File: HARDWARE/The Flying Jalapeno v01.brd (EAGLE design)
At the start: 73.7 x 72.4 mm, 96 parts, among them Q2 MMBT2222A, Q3 NDP6020P, Q4 MMBT2222A, Q5 NDP6020P, Q6 BSS138, 200mA/50V, Q7 BSS138, 200mA/50V, U1 ATMEGA2560AU, U2 LM1117, U3 LM1117, U4 LM1117, Y1 16MHZ

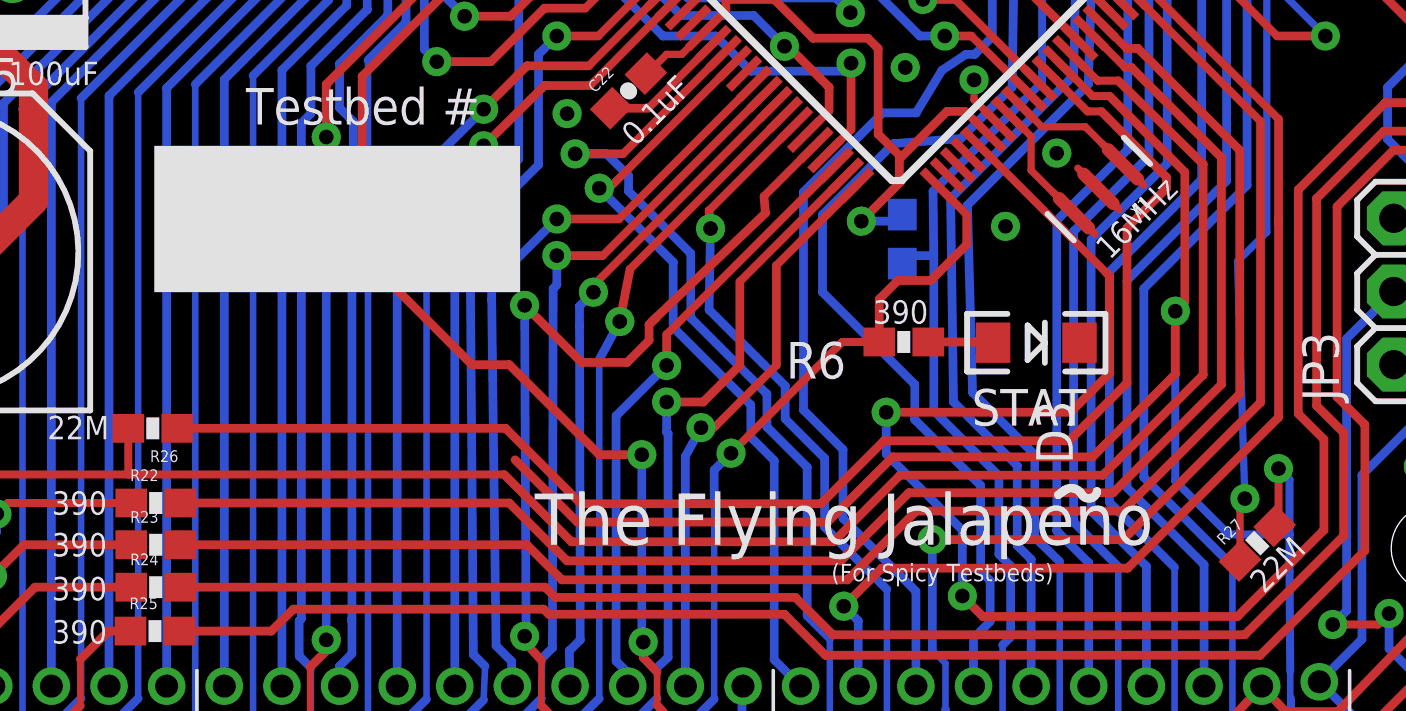
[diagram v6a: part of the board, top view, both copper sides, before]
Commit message: Fixed Rogue trace off of capsense2
Thanks for catching this in your review Kade!
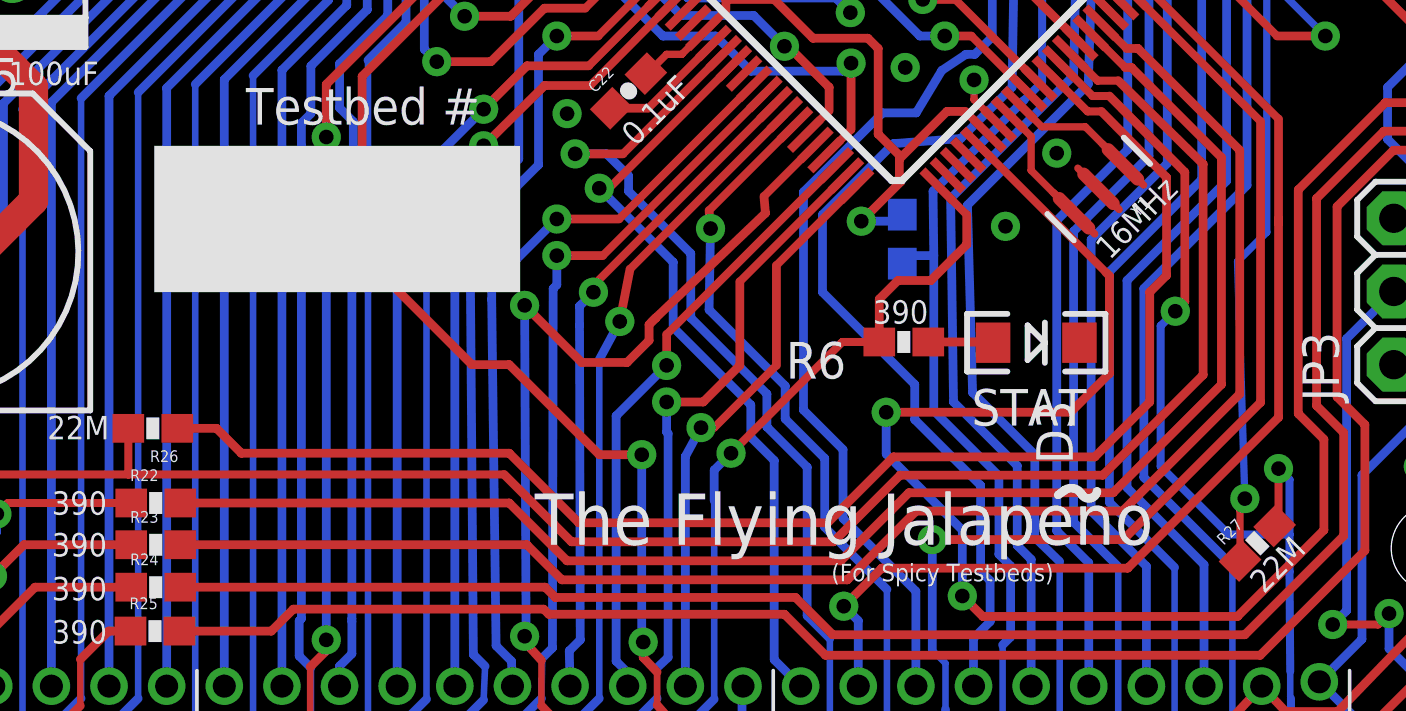
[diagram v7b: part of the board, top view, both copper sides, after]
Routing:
- net 46/CAPSENSE2: track 66.3 -> 38.6 mm
- net 47/CAPRETURN1: track 49.0 -> 50.4 mm
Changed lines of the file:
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@@
 <setting verticaltext="up"/>
 </settings>
-<grid distance="0.05" unitdist="inch" unit="inch" style="lines" multiple="1" display="yes" altdistance="0.001" altunitdist="inch" altunit="inch"/>
+<grid distance="0.05" unitdist="inch" unit="inch" style="lines" multiple="1" display="yes" altdistance="0.005" altunitdist="inch" altunit="inch"/>
 <layers>
-<layer number="1" name="Top" color="4" fill="1" visible="no" active="yes"/>
+<layer number="1" name="Top" color="4" fill="1" visible="yes" active="yes"/>
 <layer number="2" name="Route2" color="1" fill="3" visible="no" active="no"/>
 <layer number="3" name="Route3" color="4" fill="3" visible="no" active="no"/>
@@
 <layer number="14" name="Route14" color="1" fill="6" visible="no" active="no"/>
 <layer number="15" name="Route15" color="4" fill="6" visible="no" active="no"/>
-<layer number="16" name="Bottom" color="1" fill="1" visible="no" active="yes"/>
+<layer number="16" name="Bottom" color="1" fill="1" visible="yes" active="yes"/>
 <layer number="17" name="Pads" color="2" fill="1" visible="yes" active="yes"/>
 <layer number="18" name="Vias" color="2" fill="1" visible="yes" active="yes"/>
-<layer number="19" name="Unrouted" color="6" fill="1" visible="no" active="yes"/>
+<layer number="19" name="Unrouted" color="6" fill="1" visible="yes" active="yes"/>
 <layer number="20" name="Dimension" color="15" fill="1" visible="yes" active="yes"/>
 <layer number="21" name="tPlace" color="16" fill="1" visible="yes" active="yes"/>
-<layer number="22" name="bPlace" color="14" fill="1" visible="no" active="yes"/>
-<layer number="23" name="tOrigins" color="15" fill="1" visible="no" active="yes"/>
-<layer number="24" name="bOrigins" color="15" fill="1" visible="no" active="yes"/>
+<layer number="22" name="bPlace" color="14" fill="1" visible="yes" active="yes"/>
+<layer number="23" name="tOrigins" color="15" fill="1" visible="yes" active="yes"/>
+<layer number="24" name="bOrigins" color="15" fill="1" visible="yes" active="yes"/>
 <layer number="25" name="tNames" color="7" fill="1" visible="no" active="yes"/>
 <layer number="26" name="bNames" color="7" fill="1" visible="no" active="yes"/>
-<layer number="27" name="tValues" color="7" fill="1" visible="yes" active="yes"/>
+<layer number="27" name="tValues" color="7" fill="1" visible="no" active="yes"/>
 <layer number="28" name="bValues" color="7" fill="1" visible="no" active="yes"/>
 <layer number="29" name="tStop" color="7" fill="3" visible="no" active="yes"/>
 <layer number="30" name="bStop" color="7" fill="6" visible="no" active="yes"/>
-<layer number="31" name="tCream" color="7" fill="4" visible="yes" active="yes"/>
+<layer number="31" name="tCream" color="7" fill="4" visible="no" active="yes"/>
 <layer number="32" name="bCream" color="7" fill="5" visible="no" active="yes"/>
 <layer number="33" name="tFinish" color="6" fill="3" visible="no" active="yes"/>
@@
 <layer number="43" name="vRestrict" color="2" fill="10" visible="no" active="yes"/>
 <layer number="44" name="Drills" color="7" fill="1" visible="no" active="yes"/>
-<layer number="45" name="Holes" color="7" fill="1" visible="no" active="yes"/>
+<layer number="45" name="Holes" color="7" fill="1" visible="yes" active="yes"/>
 <layer number="46" name="Milling" color="3" fill="1" visible="no" active="yes"/>
 <layer number="47" name="Measures" color="7" fill="1" visible="no" active="yes"/>
@@
 <layer number="49" name="Reference" color="13" fill="1" visible="no" active="yes"/>
 <layer number="50" name="dxf" color="7" fill="1" visible="no" active="yes"/>
-<layer number="51" name="tDocu" color="6" fill="1" visible="no" active="yes"/>
+<layer number="51" name="tDocu" color="6" fill="1" visible="yes" active="yes"/>
 <layer number="52" name="bDocu" color="7" fill="1" visible="no" active="yes"/>
 <layer number="53" name="tGND_GNDA" color="7" fill="9" visible="no" active="no"/>
@@
 <contactref element="U1" pad="38"/>
 <wire x1="58.547" y1="27.1272" x2="61.1632" y2="24.4856" width="0.3048" layer="1"/>
-<wire x1="37.9222" y1="14.5034" x2="40.0812" y2="12.3444" width="0.3048" layer="1"/>
-<wire x1="40.0812" y1="12.3444" x2="48.768" y2="12.3444" width="0.3048" layer="1"/>
-<wire x1="48.768" y1="12.3444" x2="51.0286" y2="14.605" width="0.3048" layer="1"/>
-<wire x1="51.0286" y1="14.605" x2="57.9628" y2="14.605" width="0.3048" layer="1"/>
 <wire x1="56.828825" y1="28.26116875" x2="57.96279375" y2="27.1272" width="0.2794" layer="1"/>
 <wire x1="57.96279375" y1="27.1272" x2="58.547" y2="27.1272" width="0.2794" layer="1"/>
@@
 <wire x1="61.1632" y1="19.9898" x2="60.833" y2="19.6596" width="0.3048" layer="1"/>
 <via x="60.833" y="19.6596" extent="1-16" drill="0.508"/>
-<wire x1="60.833" y1="19.6596" x2="60.833" y2="13.7668" width="0.2794" layer="16"/>
-<wire x1="60.833" y1="13.7668" x2="62.6872" y2="11.9126" width="0.2794" layer="16"/>
+<wire x1="60.325" y1="14.2748" x2="62.6872" y2="11.9126" width="0.2794" layer="16"/>
 <wire x1="62.6872" y1="11.9126" x2="64.7954" y2="11.9126" width="0.2794" layer="16"/>
 <wire x1="64.7954" y1="11.9126" x2="64.7954" y2="10.6172" width="0.2794" layer="16"/>
-<wire x1="57.9628" y1="14.605" x2="60.833" y2="17.4752" width="0.3048" layer="1"/>
-<wire x1="60.833" y1="17.4752" x2="60.833" y2="19.6596" width="0.3048" layer="1"/>
 <contactref element="JP4" pad="58"/>
 <wire x1="61.83" y1="2.14" x2="61.83" y2="1" width="0.3048" layer="16"/>
+<wire x1="60.325" y1="14.2748" x2="60.325" y2="19.1516" width="0.2794" layer="16"/>
+<wire x1="60.325" y1="19.1516" x2="60.833" y2="19.6596" width="0.2794" layer="16"/>
 </signal>
 <signal name="47/CAPRETURN1">
 <contactref element="U1" pad="37"/>
 <contactref element="R26" pad="1"/>
-<wire x1="59.1566" y1="22.5552" x2="60.5282" y2="23.9268" width="0.3048" layer="1"/>
 <wire x1="58.2676" y1="26.5938" x2="60.5282" y2="24.3078" width="0.3048" layer="1"/>
-<wire x1="60.5282" y1="24.3078" x2="60.5282" y2="23.9268" width="0.3048" layer="1"/>
-<wire x1="26.1992" y1="15.5956" x2="37.592" y2="15.5956" width="0.3048" layer="1"/>
-<wire x1="37.592" y1="15.5956" x2="40.2082" y2="12.9794" width="0.3048" layer="1"/>
-<wire x1="40.2082" y1="12.9794" x2="48.5394" y2="12.9794" width="0.3048" layer="1"/>
-<wire x1="48.5394" y1="12.9794" x2="50.7238" y2="15.1638" width="0.3048" layer="1"/>
-<wire x1="50.7238" y1="15.1638" x2="57.15" y2="15.1638" width="0.3048" layer="1"/>
+<wire x1="26.1992" y1="15.5956" x2="27.559" y2="15.5956" width="0.3048" layer="1"/>
 <wire x1="56.475271875" y1="27.907615625" x2="57.7890875" y2="26.5938" width="0.2794" layer="1"/>
 <wire x1="57.7890875" y1="26.5938" x2="58.2676" y2="26.5938" width="0.2794" layer="1"/>
-<wire x1="59.1566" y1="22.5552" x2="59.1566" y2="17.1704" width="0.3048" layer="1"/>
-<wire x1="59.1566" y1="17.1704" x2="57.15" y2="15.1638" width="0.3048" layer="1"/>
+<wire x1="60.5282" y1="24.3078" x2="60.5282" y2="20.9042" width="0.3048" layer="1"/>
+<wire x1="60.5282" y1="20.9042" x2="59.944" y2="20.32" width="0.3048" layer="1"/>
+<wire x1="59.944" y1="20.32" x2="59.944" y2="16.51" width="0.3048" layer="1"/>
+<wire x1="59.944" y1="16.51" x2="58.039" y2="14.605" width="0.3048" layer="1"/>
+<wire x1="58.039" y1="14.605" x2="51.054" y2="14.605" width="0.3048" layer="1"/>
+<wire x1="51.054" y1="14.605" x2="48.768" y2="12.319" width="0.3048" layer="1"/>
+<wire x1="48.768" y1="12.319" x2="40.132" y2="12.319" width="0.3048" layer="1"/>
+<wire x1="40.132" y1="12.319" x2="37.719" y2="14.732" width="0.3048" layer="1"/>
+<wire x1="37.719" y1="14.732" x2="28.4226" y2="14.732" width="0.3048" layer="1"/>
+<wire x1="28.4226" y1="14.732" x2="27.559" y2="15.5956" width="0.3048" layer="1"/>
 </signal>
 <signal name="48/PWR_CTRL1">
